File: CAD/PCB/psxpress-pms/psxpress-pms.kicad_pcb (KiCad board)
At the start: 2 copper layers, 35.9 x 35.9 mm, 41 parts, among them IC1 BQ25606RGER, IC2 MAX16054AZT+T, IC3 TPS61023DRLT, IC4 TPS564255DRLR, Q1 AONR21117

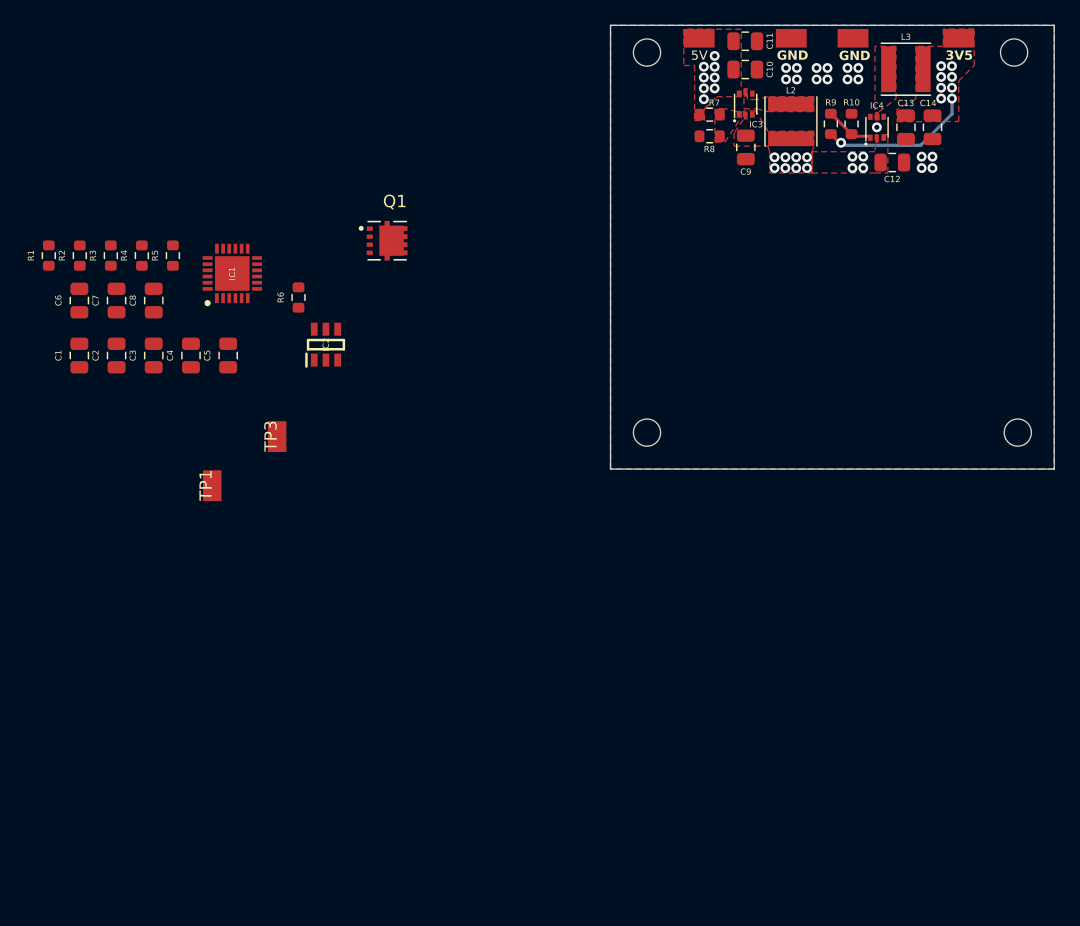
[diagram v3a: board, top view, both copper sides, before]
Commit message: pms - route BQ chip, finalize board footprint, & start optimizing
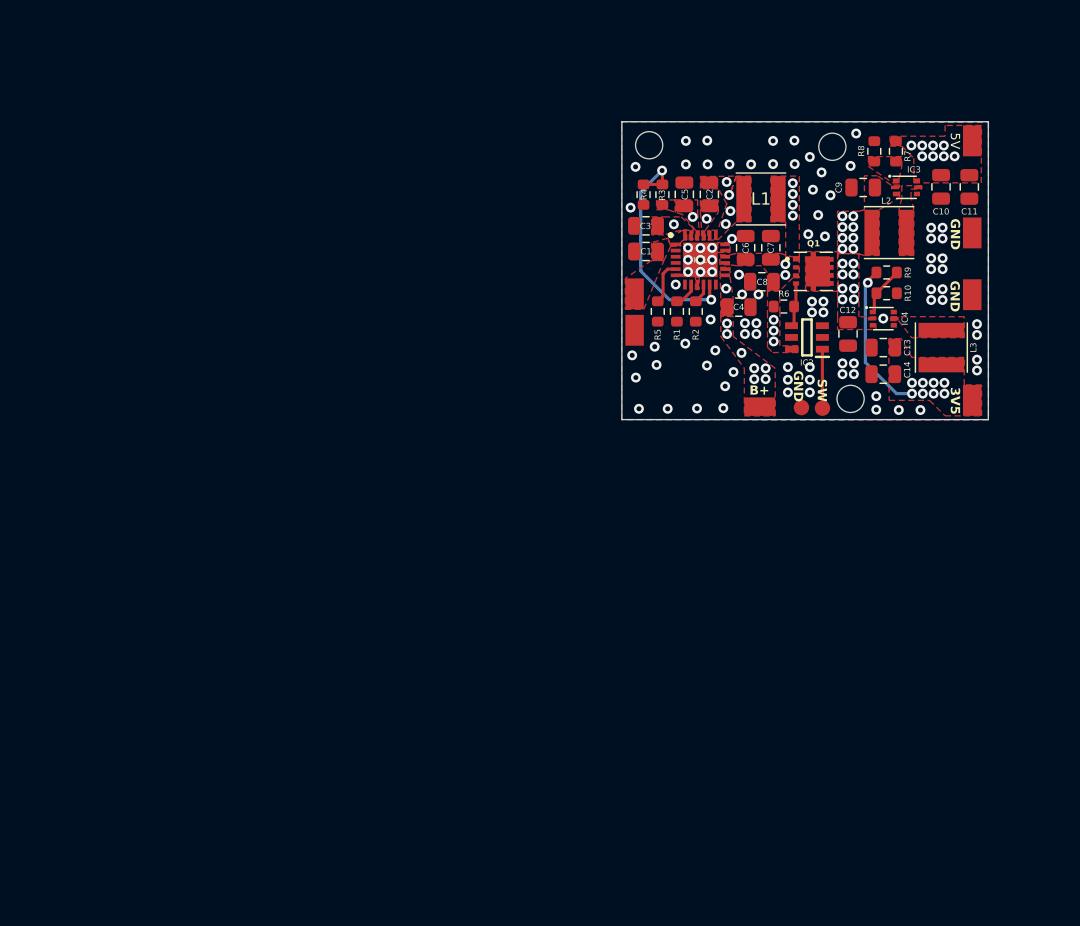
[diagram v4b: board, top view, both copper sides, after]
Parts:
- removed the REF** at (159.4, 81.8)
- added L1: 1uH, Inductor_SMD:L_Taiyo-Yuden_MD-4040, F.Cu at (168.7, 62.9)
- added SW1: SW_SPST, solderpads:pwr_switch_1.25mm_2, F.Cu at (172.8, 79.8)
- added TP2: VBUS, solderpads:hipower_2.5x1.5mm, F.Cu at (158.4, 70.6)
- TP1, TP3, TP5, TP6, TP7, TP8: footprint solderpads:power_pad_2.5x1.5mm -> solderpads:hipower_2.5x1.5mm
- moved C6 54.1 mm to (167.4, 66.9)
- moved C7 53.1 mm to (169.5, 66.9)
- moved R1 51.0 mm to (161.9, 72.0)
- moved R2 50.0 mm to (163.4, 72.0)
- moved C2 49.7 mm to (164.5, 62.5), turned to -90 degrees
- moved C8 49.2 mm to (168.7, 69.6), turned to 180 degrees
- moved C1 46.6 mm to (159.4, 67.2), turned to 180 degrees
- moved R3 44.9 mm to (160.7, 62.6)
- moved C4 44.5 mm to (166.9, 71.7), turned to 0 degrees
- moved C3 41.2 mm to (159.4, 65.1), turned to 180 degrees
- moved R4 40.9 mm to (159.2, 62.6), turned to -90 degrees
- moved R5 39.5 mm to (160.3, 72.0), turned to -90 degrees
- moved R6 39.3 mm to (170.5, 71.6), turned to 180 degrees
- moved TP3 39.2 mm to (168.6, 79.7), turned to 0 degrees
- moved C5 39.1 mm to (162.5, 62.5), turned to -90 degrees
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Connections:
- Q1 pad 1: Net-(IC2-~{OUT}) -> VOUT
- Q1 pad 3: VSYS -> VOUT
- Q1 pad 4: (no net) -> Net-(IC2-~{OUT})
- Q1 pad 5: (no net) -> VSYS
- Q1 pad 6: (no net) -> VSYS
- Q1 pad 7: (no net) -> VSYS
- Q1 pad 8: (no net) -> VSYS
- Q1 pad 9: (no net) -> VSYS
- Q1 pad 9_1: (no net) -> VSYS
- Q1 pad 9_2: (no net) -> VSYS
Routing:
- net Net-(IC1-TS): track 0.00 -> 19.4 mm, vias 0 -> 2
- net Net-(IC2-IN): track 0.00 -> 4.78 mm
- net STAT: track 0.00 -> 3.58 mm
- net Net-(IC2-~{OUT}): track 0.00 -> 3.57 mm
- net Net-(IC1-ILIM): track 0.00 -> 2.03 mm
- net Net-(IC1-ICHG): track 0.00 -> 1.61 mm
- net GND: track 0.21 -> 1.33 mm, vias 17 -> 88
- net Net-(IC1-REGN): track 0.00 -> 0.28 mm, vias 0 -> 1
- net VOUT: track 0.00 -> 0.22 mm, vias 0 -> 9
- net VSYS: vias 12 -> 16
- net Net-(IC1-PMID): vias 0 -> 1
- net Net-(IC1-BTST): vias 0 -> 1
- net Net-(C4-Pad1): vias 0 -> 8
- net Net-(C2-Pad1): vias 0 -> 4
- added copper zone on F.Cu, net Net-(C2-Pad1)
- added copper zone on F.Cu, net Net-(C4-Pad1)
- added copper zone on F.Cu, net Net-(IC1-BTST)
- added copper zone on F.Cu, net Net-(IC1-PMID)
- added copper zone on F.Cu, net Net-(IC1-REGN)
- added copper zone on F.Cu, net Net-(IC1-VAC)
- added copper zone on F.Cu, net VOUT
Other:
- board size 35.9 x 35.9 mm -> 29.7 x 24.1 mm
- board text added: "B+"
- board text added: "BitBuilt 2023 Summer Building Contest"
- board text added: "PSXpress"
- board text added: "Power Management System"
- board text added: "SW"

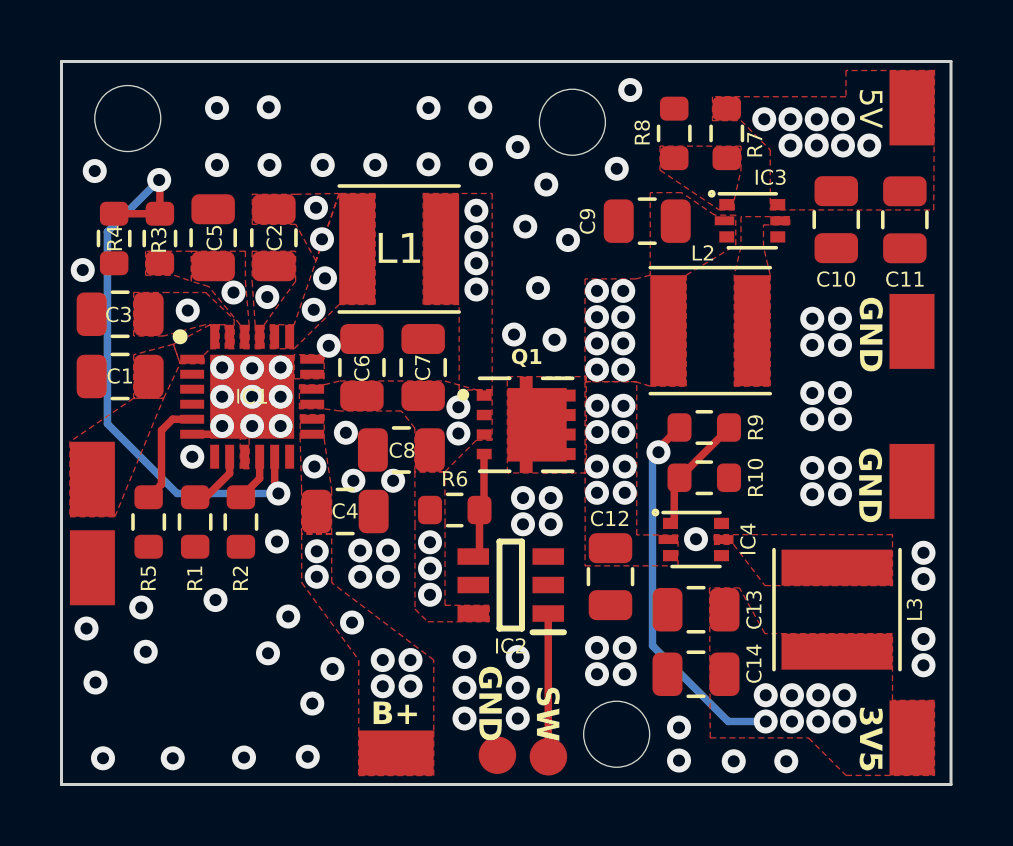
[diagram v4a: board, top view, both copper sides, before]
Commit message: pms - finish optimizing  - board complete
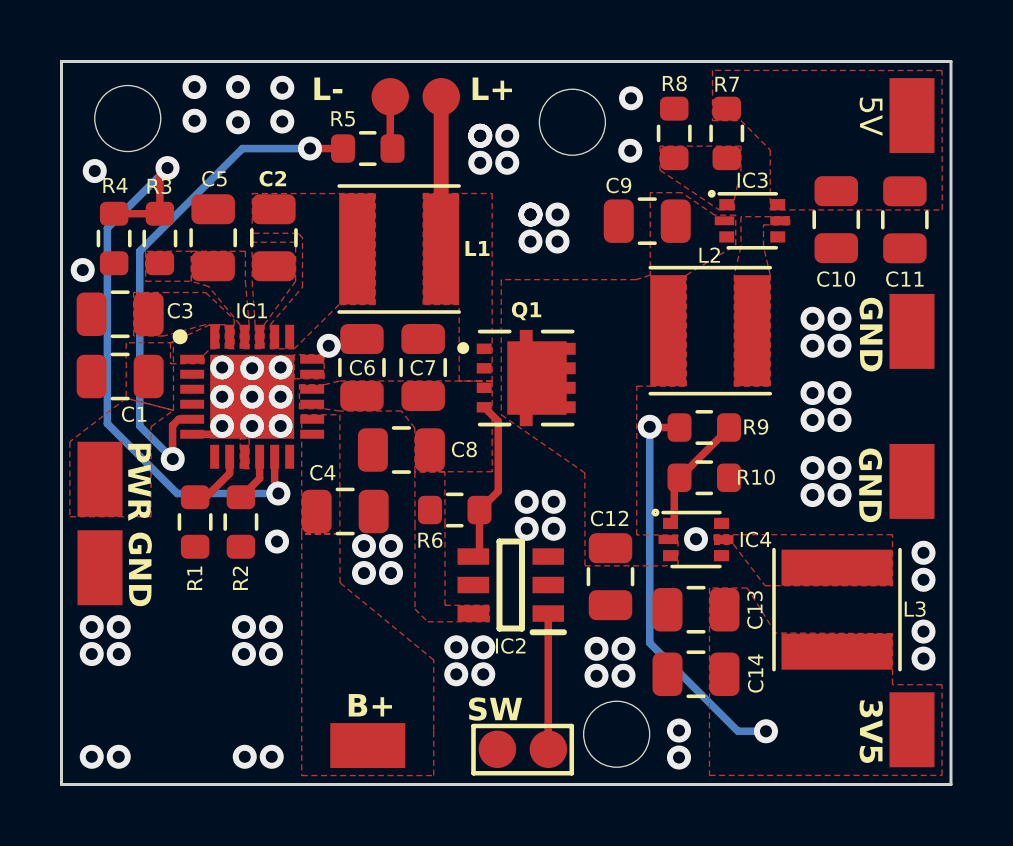
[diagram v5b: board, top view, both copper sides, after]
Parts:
- added D1: LED, solderpads:led_1.25mm_2, F.Cu at (169.2, 57.8)
- R1: value 226 -> 150
- R2: value 402 -> 226
- moved R5 14.4 mm to (167.6, 59.6), turned to 0 degrees
- moved Q1 1.56 mm to (172.9, 67.2)
- moved TP3 0.98 mm to (167.7, 79.5)
- moved TP6 0.27 mm to (185.8, 79.0)
- moved TP5 0.25 mm to (185.8, 58.5)
- moved TP1 0.25 mm to (158.7, 73.5)
- moved TP2 0.25 mm to (158.7, 70.6)
- moved SW1 0.25 mm to (172.8, 79.5)
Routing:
- net STAT: track 3.58 -> 17.4 mm, vias 0 -> 2
- net VOUT: track 0.22 -> 5.30 mm, vias 9 -> 0
- net Net-(IC2-~{OUT}): track 3.57 -> 5.51 mm
- net Net-(D1-K): track 0.00 -> 1.76 mm
- net Net-(IC1-TS): track 19.4 -> 20.4 mm
- net +3.5V: track 12.5 -> 13.3 mm, vias 9 -> 2
- net GND: vias 88 -> 78
- net VSYS: vias 16 -> 0
- net Net-(IC1-REGN): vias 1 -> 0
- net Net-(IC1-PMID): vias 1 -> 0
- net Net-(IC1-BTST): vias 1 -> 0
- net Net-(C4-Pad1): vias 8 -> 0
- net Net-(C2-Pad1): vias 4 -> 0
- net +5V: vias 8 -> 0
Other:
- board text added: "BitBuilt 2023 Summer Building Contest https://github.com/Y2K-x"
- board text added: "L+"
- board text added: "L-"
- board text added: "PWR"
- board text removed: "BitBuilt 2023 Summer Building Contest"
